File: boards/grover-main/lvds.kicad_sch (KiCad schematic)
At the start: 1 part

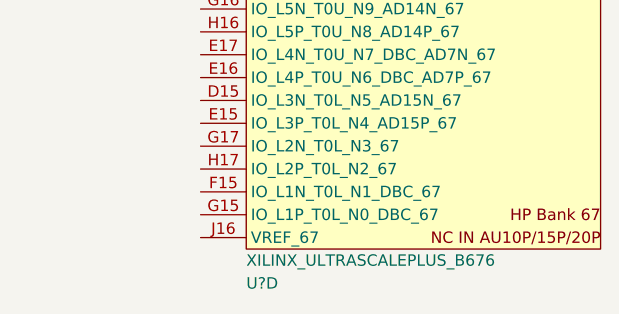
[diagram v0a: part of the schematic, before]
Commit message: Continued initial schematic capture
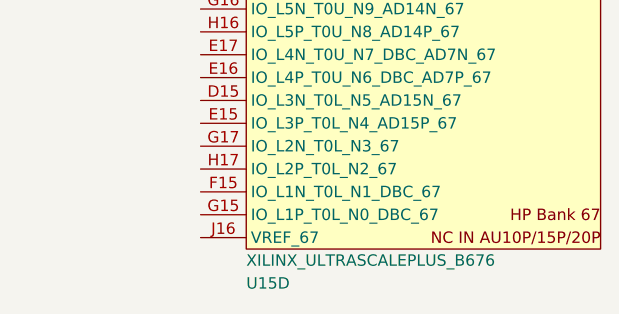
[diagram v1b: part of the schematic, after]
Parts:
- gave numbers to parts that had none: 1
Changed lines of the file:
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@@
   (symbol (lib_id "xilinx-azonenberg:XILINX_ULTRASCALEPLUS_B676") (at 66.04 166.37 0) (unit 4)
     (in_bom yes) (on_board yes)
-    (property "Reference" "U?" (id 0) (at 66.04 170.18 0)
+    (property "Reference" "U15" (id 0) (at 66.04 170.18 0)
       (effects (font (size 1.27 1.27)) (justify left))
     )
